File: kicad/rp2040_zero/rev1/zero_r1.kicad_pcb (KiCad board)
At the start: 2 copper layers, 41.8 x 30.2 mm, 19 parts, among them J1 jtag, J2 Conn_01x03_Socket, J5 Debug port, U1 RP2040-Zero, U3 3V->VTREF, U4 VTREF->3V, U5 VTREF<->3V, U6 RT9013-33GB

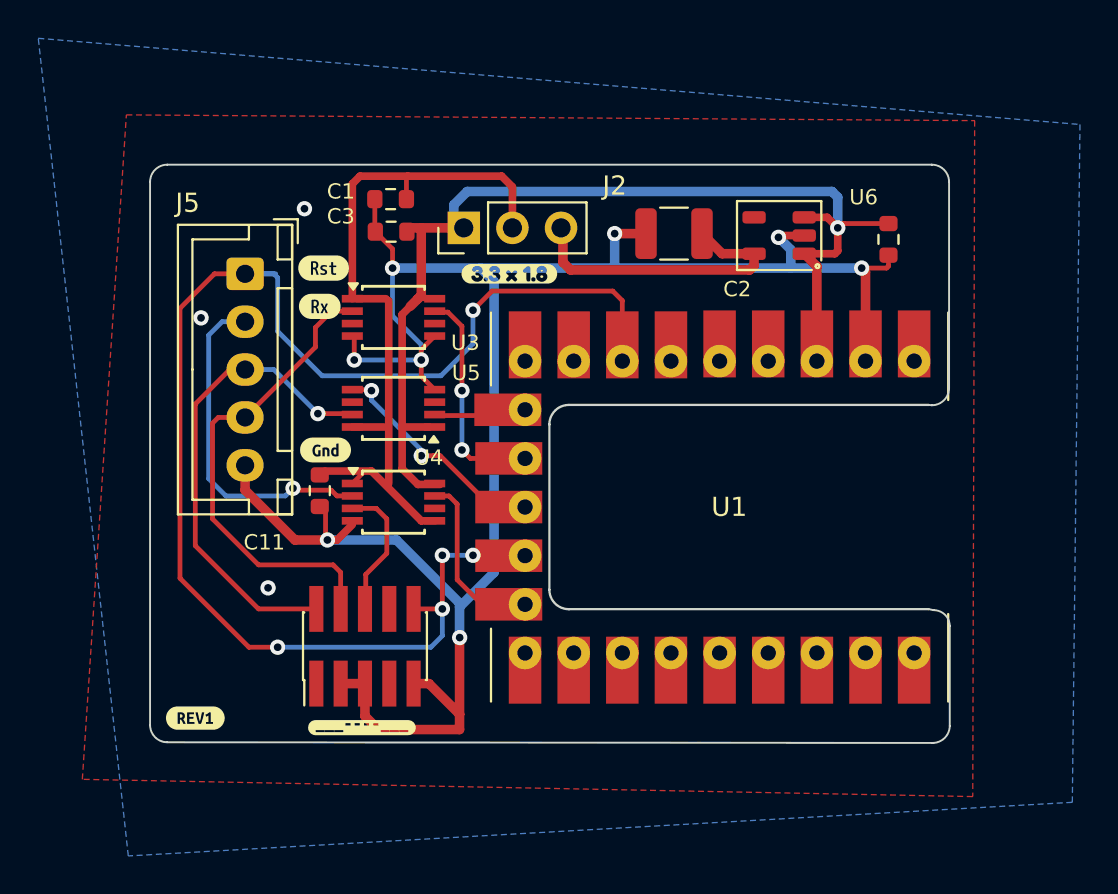
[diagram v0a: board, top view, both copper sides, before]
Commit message: kicad : add debug port for rp2xxx carrier board
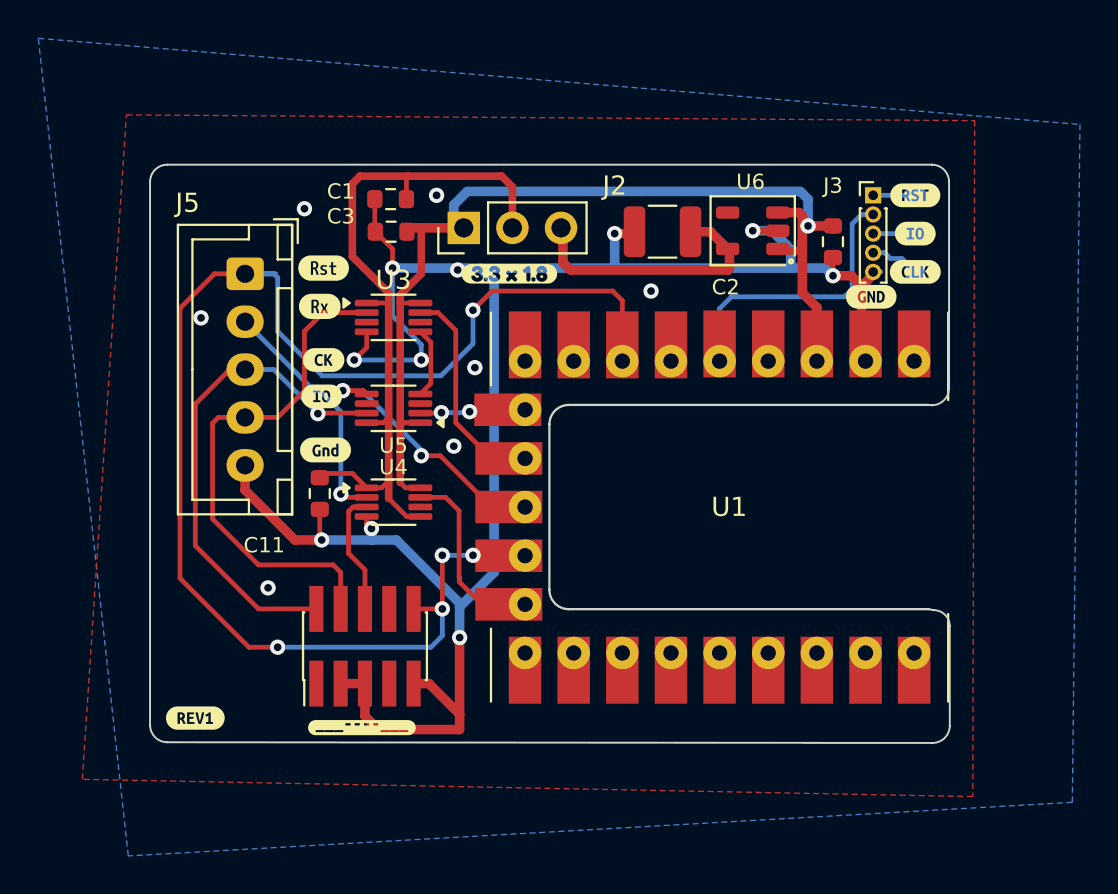
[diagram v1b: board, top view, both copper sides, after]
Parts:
- added J3: Debug port, Connector_PinHeader_1.00mm:PinHeader_1x05_P1.00mm_Vertical, F.Cu at (146.1, 67.9)
- added REF**: TestPoint_Pad_1.0x1.0mm, TestPoint:TestPoint_Pad_1.0x1.0mm, B.Cu at (148.3, 69.9)
- added REF**: TestPoint_Pad_1.0x1.0mm, TestPoint:TestPoint_Pad_1.0x1.0mm, B.Cu at (148.3, 67.9)
- added REF**: TestPoint_Pad_1.0x1.0mm, TestPoint:TestPoint_Pad_1.0x1.0mm, B.Cu at (148.3, 71.9)
- added kibuzzard-67D71CE3: G***, kibuzzard-67D71CE3, F.Cu at (148.3, 69.9)
- added kibuzzard-67D71D2A: G***, kibuzzard-67D71D2A, F.Cu at (148.3, 67.9)
- added kibuzzard-67D71D3A: G***, kibuzzard-67D71D3A, F.Cu at (148.3, 71.9)
- added kibuzzard-67D71D53: G***, kibuzzard-67D71D53, F.Cu at (146.0, 73.2)
- added kibuzzard-67D71DD3: G***, kibuzzard-67D71DD3, F.Cu at (117.3, 78.4)
- added kibuzzard-67D71DDE: G***, kibuzzard-67D71DDE, F.Cu at (117.4, 76.5)
- U3, U4, U5: footprint Package_SO:TSSOP-8_3x3mm_P0.65mm -> Package_SO:VSSOP-8_2.3x2mm_P0.5mm
- moved C10 2.90 mm to (144.0, 70.3)
- moved U6 1.40 mm to (139.8, 69.7)
- moved C2 0.61 mm to (135.1, 69.8)
- moved C11 0.15 mm to (117.2, 83.5)
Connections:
- U1 pad 5: unconnected-(U1-GP28-Pad5) -> UART_TX
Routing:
- net UART_TX: track 0.00 -> 14.8 mm
- net OUT_UART_RX: track 18.1 -> 12.7 mm
- net +3.3V: track 56.7 -> 53.1 mm
- net SWDCLK: track 0.00 -> 2.61 mm
- net SWDIO: track 0.00 -> 2.20 mm
- net NRST: track 0.00 -> 2.20 mm
- net V1.8: track 15.8 -> 13.6 mm
- net OUT_SWDCLK: track 25.1 -> 27.0 mm
- net SWIO_DIR_3V: track 10.3 -> 11.8 mm
- net GND: track 110.5 -> 112.0 mm, vias 11 -> 17
- net VTREF: track 39.1 -> 37.7 mm
- net OUT_SWDCLK_3V: track 10.7 -> 9.70 mm, vias 2 -> 0
- net OUT_SWDIO_3V: track 3.49 -> 2.61 mm, vias 0 -> 2
- net OUT_SWDIO: track 24.1 -> 24.9 mm
- net INOUT_SWO: track 7.14 -> 6.49 mm
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
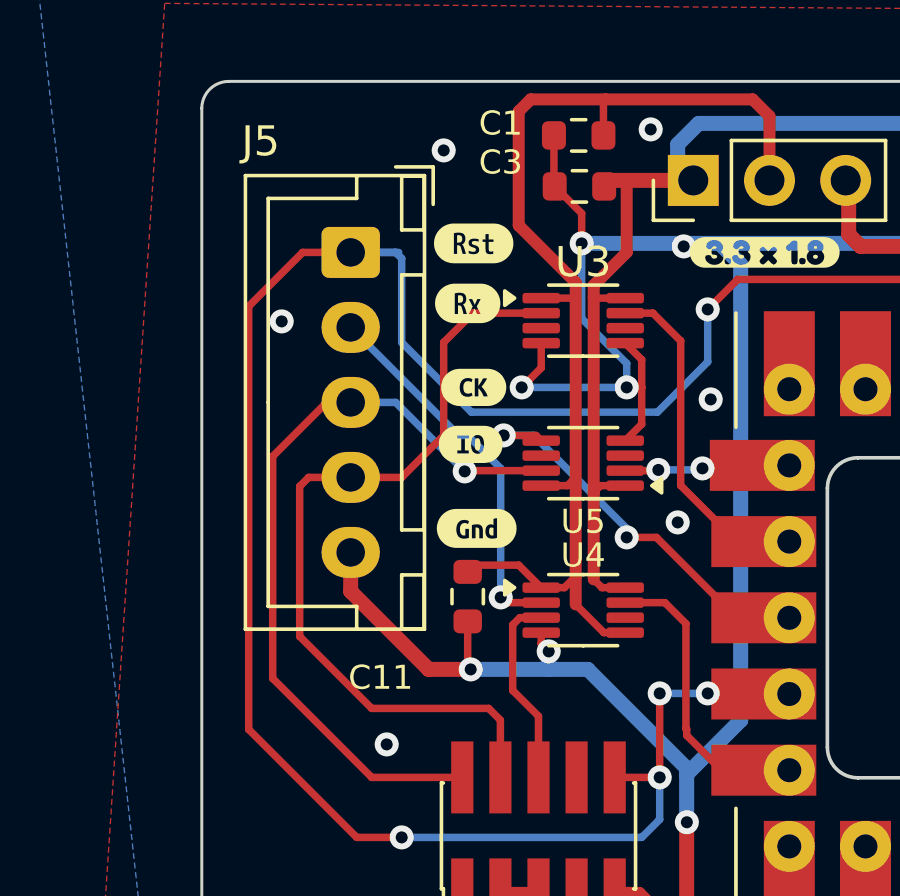
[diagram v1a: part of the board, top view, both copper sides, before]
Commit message: rp2040: update pcb, add optional pullup
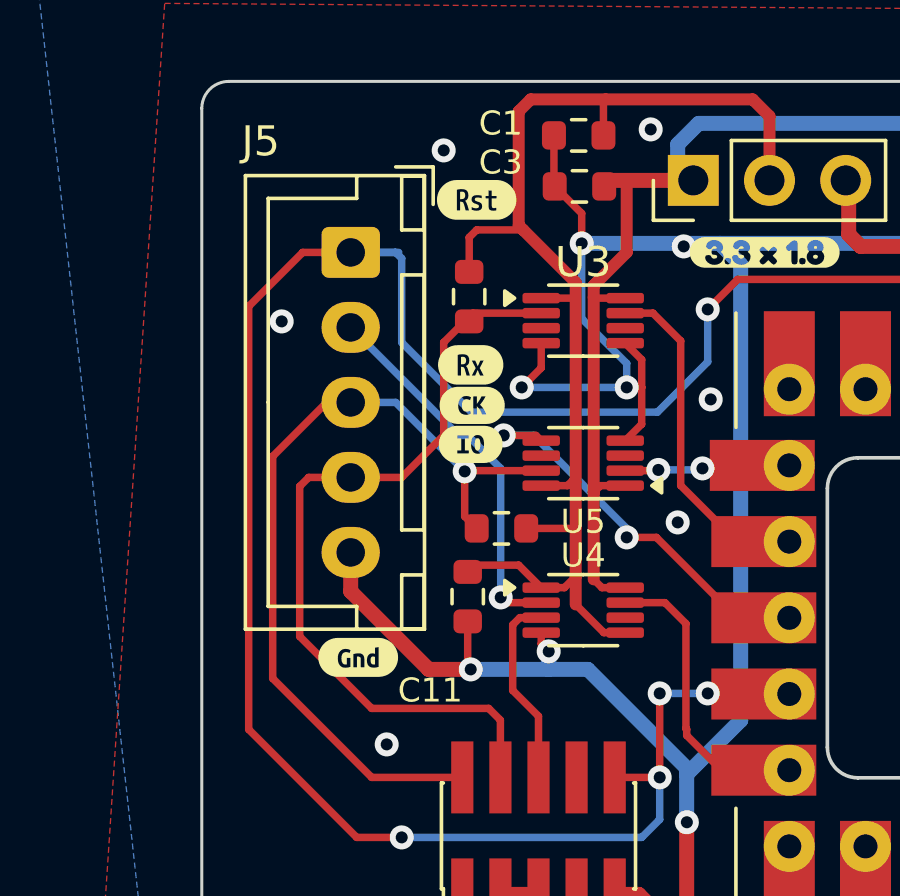
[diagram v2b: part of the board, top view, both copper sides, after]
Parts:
- added PULLUP: R_0603_1608Metric, Resistor_SMD:R_0603_1608Metric, F.Cu at (118.3, 81.2)
- added PULLUP2: R_0603_1608Metric, Resistor_SMD:R_0603_1608Metric, F.Cu at (117.3, 73.5)
- moved kibuzzard-67A3B7A3 5.84 mm to (113.6, 85.5)
- moved kibuzzard-67310DA4 2.05 mm to (117.3, 75.7)
- moved kibuzzard-67310D89 1.45 mm to (117.5, 70.2)
- moved kibuzzard-67D71DDE 0.60 mm to (117.4, 77.1)
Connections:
- U1 pad 5: UART_TX -> unconnected-(U1-GP28-Pad5)
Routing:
- net VTREF: track 37.7 -> 42.4 mm
- net OUT_SWDIO: track 24.9 -> 27.0 mm
